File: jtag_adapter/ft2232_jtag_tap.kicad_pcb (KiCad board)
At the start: 2 copper layers, 50 x 34 mm, 72 parts, among them J1 USB_C_Receptacle_USB2.0, J2 Conn_ARM_JTAG_SWD_20, Q1 BSS138, Q2 BSS138, U1 N.F./93AA56BT-I/OT, U2 SIT2001B, U3 FT232HL, U4 SN74AXCH4T245PW, U5 SN74AXCH4T245PW, U6 SN74AXCH1T45

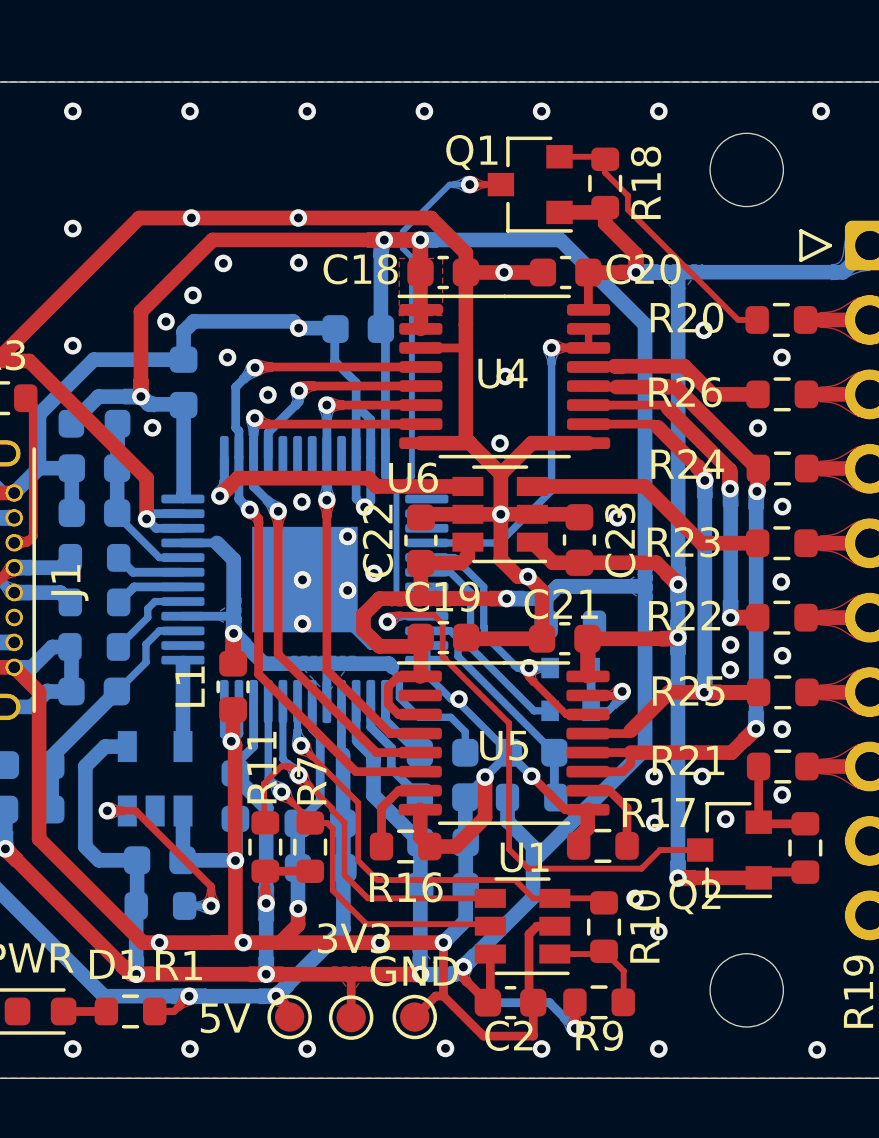
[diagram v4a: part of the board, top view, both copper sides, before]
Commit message: wip: remove JTAG_EN pin
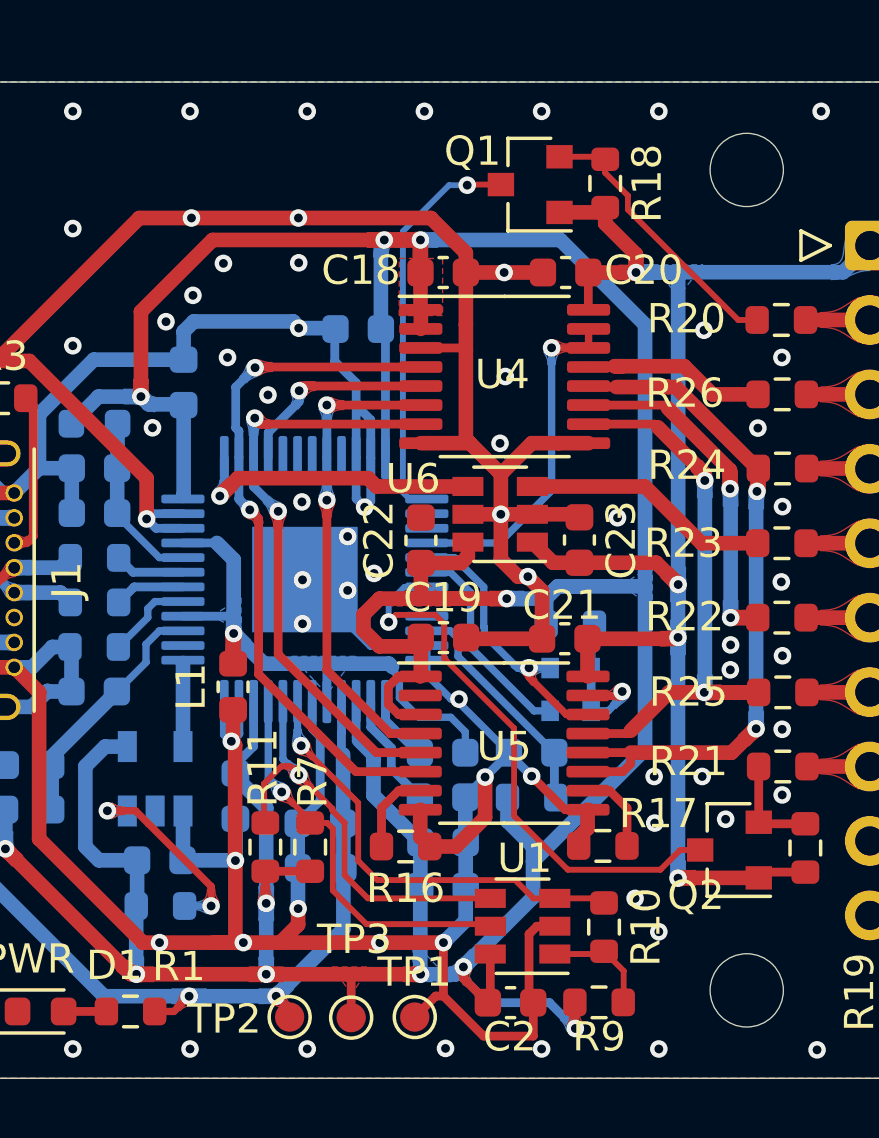
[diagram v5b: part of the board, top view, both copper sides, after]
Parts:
- U6: value SN74AXCH1T45 -> SN74AXCH1T45DBVR
- renumbered GND to TP1, 5V to TP2, 3V3 to TP3
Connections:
- U3 pad 25: (no net) -> /ft232hl/JTAG_nTRST
- U3 pad 31: (no net) -> /ft232hl/JTAG_nSRST
- U3 pad 32: /ft232hl/JTAG_nTRST -> (no net)
- U3 pad 33: /ft232hl/JTAG_nSRST -> (no net)
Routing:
- net /ft232hl/JTAG_nTRST: track 17.9 -> 13.8 mm
- net GND: track 209.0 -> 207.4 mm

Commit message: wip: stash
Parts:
- removed D4, D5: CDSU101A, Diode_SMD:D_SOD-523
- removed R15, R16, R17: 10k, Resistor_SMD:R_0603_1608Metric
- added C24: 0.1uF, Capacitor_SMD:C_0603_1608Metric, B.Cu at (77.1, 121.4)
- added U7: SN74LVC2G00DCUT, Package_SO:VSSOP-8_2.3x2mm_P0.5mm, B.Cu at (75.5, 119.3)
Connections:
- U3 pad 28: /ft232hl/JTAG_EN -> (no net)
- U4 pad 14: /ft232hl/JTAG_EN -> /ft232hl/SWD_EN
- U4 pad 15: /ft232hl/JTAG_EN -> /ft232hl/SWD_EN
- U5 pad 10: Net-(R17-Pad1) -> (no net)
- U5 pad 14: /ft232hl/SWD_EN -> /jtag/~SWD_OE
- U5 pad 15: Net-(D4-Pad2) -> /jtag/~SWD_EN
- U5 pad 7: Net-(R16-Pad2) -> (no net)
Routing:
- net GND: track 207.4 -> 221.7 mm, vias 105 -> 115
- net /ft232hl/SWD_EN: track 9.59 -> 23.0 mm
- net /ft232hl/JTAG_EN: track 11.8 -> 0.00 mm, vias 1 -> 0
- net Net-(D4-Pad2): track 5.67 -> 0.00 mm, vias 1 -> 0
- net +3V3: track 154.2 -> 159.1 mm
- net /jtag/~SWD_OE: track 0.00 -> 4.07 mm, vias 0 -> 1
- net /jtag/~SWD_EN: track 0.00 -> 3.78 mm, vias 0 -> 1
- net Net-(R16-Pad2): track 2.88 -> 0.00 mm
- net Net-(R17-Pad1): track 2.87 -> 0.00 mm
- net /ft232hl/SWDIO_OE: track 7.27 -> 4.82 mm
- net /ft232hl/JTAG_nSRST: track 19.2 -> 18.7 mm
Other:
- board text added: "jtag adapter v1.1(2022.01.16) @tnishinaga"
- board text removed: "jtag adapter v1.0(2021.09.03) @tnishinaga"
